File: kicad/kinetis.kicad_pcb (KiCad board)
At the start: 2 copper layers, 70 parts, among them J1 CONN_01X16, J2 CONN_01X16, J3 CONN_01X16, J4 CONN_01X16, J5 USB_Micro_B, J6 FTDI_Connector, J7 JLink_SWD_20pin, SW1 SPST, SW2 SPST, SW3 SPST, SW4 SPST, SW5 SPST, SW6 DPDT, U1 MKL16Z64VLH4, U2 LM1117-ADJ, Y1 12.000 MHz

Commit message: Lots of component placement. More to go.
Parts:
- moved C6 197.0 mm to (348.7, 85.3)
- moved R14 197.0 mm to (332.2, 112.0)
- moved R16 197.0 mm to (344.9, 96.8)
- moved R17 197.0 mm to (332.2, 122.2)
- moved R8 197.0 mm to (348.7, 117.1)
- moved C1 197.0 mm to (321.3, 132.3)
- moved C2 197.0 mm to (305.6, 86.6)
- moved C3 197.0 mm to (341.1, 86.6)
- moved R1 197.0 mm to (332.5, 106.9)
- moved R10 197.0 mm to (314.5, 134.9)
- moved R11 197.0 mm to (337.3, 98.0)
- moved R12 197.0 mm to (303.3, 106.9)
- moved R13 197.0 mm to (337.3, 91.7)
- moved R15 197.0 mm to (338.8, 123.4)
- moved R18 197.0 mm to (335.0, 117.1)
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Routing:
- added copper zone on F.Cu, net GND
- added copper zone on In1.Cu, net GND
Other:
- copper layers 2 -> 4

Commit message: Updated placement. More to go still.
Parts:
- moved R9 303.8 mm to (47.2, 128.3)
- moved R8 300.6 mm to (48.3, 123.7)
- moved C4 295.9 mm to (80.0, 75.4), turned to 90 degrees
- moved R7 293.4 mm to (48.3, 119.4)
- moved R16 273.0 mm to (73.9, 129.5)
- moved R22 269.8 mm to (61.7, 129.8)
- moved C6 269.1 mm to (80.0, 70.4), turned to 270 degrees
- moved R10 266.5 mm to (48.0, 132.1)
- moved R17 264.0 mm to (68.3, 129.5)
- moved R11 262.6 mm to (85.3, 24.1)
- moved C3 261.2 mm to (80.0, 78.2), turned to 270 degrees
- moved R6 258.8 mm to (93.5, 119.6)
- moved R21 256.8 mm to (55.9, 129.5)
- moved R13 245.7 mm to (94.0, 125.7)
- moved R14 239.0 mm to (94.0, 130.8)
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
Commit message: More placement and some preliminary routing
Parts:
- moved R10 84.7 mm to (110.7, 75.2)
- moved R14 77.6 mm to (83.2, 54.0)
- moved R8 77.0 mm to (110.7, 78.7)
- moved R9 76.6 mm to (110.7, 85.3)
- moved R13 75.3 mm to (75.6, 52.7)
- moved R7 72.7 mm to (110.7, 82.3)
- moved R6 51.9 mm to (110.1, 70.5)
- moved C12 38.7 mm to (64.8, 64.0), turned to 270 degrees
- moved C11 32.1 mm to (61.0, 63.8), turned to 270 degrees
- moved R5 29.8 mm to (110.5, 89.5)
- moved SW4 27.8 mm to (68.4, 128.4)
- moved R21 25.8 mm to (77.9, 116.0)
- moved R16 21.3 mm to (68.7, 108.8), turned to 180 degrees
- moved SW1 18.0 mm to (68.5, 114.0), turned to 180 degrees
- moved C10 17.5 mm to (47.0, 63.5), turned to 90 degrees
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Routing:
- net +3V3: track 0.00 -> 54.2 mm
- net GND: track 0.00 -> 13.3 mm, vias 0 -> 8
- net /SW[W]: track 0.00 -> 13.3 mm
- net /SW[E]: track 0.00 -> 11.6 mm
- net /SW[S]: track 0.00 -> 11.3 mm
- net /SW[N]: track 0.00 -> 10.8 mm
- net Net-(D4-PadK): track 0.00 -> 8.38 mm
- net Net-(D3-PadK): track 0.00 -> 8.38 mm
- net Net-(D2-PadK): track 0.00 -> 8.38 mm
- net Net-(D1-PadK): track 0.00 -> 8.38 mm
- added copper zone on B.Cu, net GND
- removed copper zone on F.Cu, net GND
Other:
- net class Default: clearance 0.2 -> 0.254; trace_width 0.25 -> 0.254; via_dia 0.6 -> 0.6096; via_drill 0.4 -> 0.3048
- rule trace_clearance: 0.2 -> 0.254
- rule trace_min: 0.2 -> 0.1524
- rule via_min_drill: 0.3 -> 0.3048
- rule via_min_size: 0.4 -> 0.6096
- board text added: "[0]"
- board text added: "[1]"
- board text added: "[2]"
- board text added: "[3]"

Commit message: Lots of layout and placement changes.
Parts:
- moved R11 90.4 mm to (170.2, 55.2)
- moved J6 87.9 mm to (96.5, 123.8)
- moved R1 87.9 mm to (106.7, 128.9)
- moved R2 87.9 mm to (102.9, 128.9)
- moved R3 87.9 mm to (99.1, 128.7)
- moved R4 87.9 mm to (110.5, 128.9)
- moved J7 84.9 mm to (174.6, 62.2)
- moved J5 83.1 mm to (123.8, 57.1)
- moved R12 82.9 mm to (164.5, 55.2)
- moved R6 79.6 mm to (176.5, 114.3), turned to 180 degrees
- moved R8 72.5 mm to (176.5, 109.2), turned to 180 degrees
- moved R7 72.1 mm to (176.5, 111.8), turned to 180 degrees
- moved R10 71.9 mm to (176.5, 104.1), turned to 180 degrees
- moved R5 71.5 mm to (176.5, 116.8), turned to 180 degrees
- moved R9 69.2 mm to (176.5, 106.7), turned to 180 degrees
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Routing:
- net /HEADER_C[3]: track 0.00 -> 33.8 mm
- net /HEADER_C[4]: track 0.00 -> 32.7 mm
- net /HEADER_C[5]: track 0.00 -> 30.9 mm
- net +3V3: track 54.2 -> 23.4 mm, vias 0 -> 3
- net /HEADER_C[6]: track 0.00 -> 29.3 mm
- net /HEADER_C[7]: track 0.00 -> 27.2 mm
- net /HEADER_C[8]: track 0.00 -> 26.2 mm
- net /HEADER_A[1]: track 0.00 -> 25.4 mm
- net /HEADER_D[16]: track 0.00 -> 25.2 mm
- net /HEADER_B[1]: track 0.00 -> 25.2 mm
- net /HEADER_D[1]: track 0.00 -> 24.8 mm
- net /HEADER_B[2]: track 0.00 -> 24.4 mm
- net /HEADER_D[15]: track 0.00 -> 24.0 mm
- net /HEADER_A[2]: track 0.00 -> 24.0 mm
- net /HEADER_D[2]: track 0.00 -> 24.0 mm
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
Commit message: Misc pin tweaks. Lots more routing.
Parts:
- removed R15, R18, R19, R20: 200, custom_footprints:SM_0805
- added C13: 0.1uF, custom_footprints:SM_0603, F.Cu at (132.1, 71.1)
- added C14: 0.1uF, custom_footprints:SM_0603, F.Cu at (124.5, 71.1)
- added C15: 0.1uF, custom_footprints:SM_0603, F.Cu at (177.3, 121.4)
- added C16: 0.1uF, custom_footprints:SM_0603, F.Cu at (174.8, 121.4)
- R13, R14, R5, R6: value 0.1 -> 200
- moved R11 32.1 mm to (142.2, 71.1), turned to 270 degrees
- moved R12 32.0 mm to (137.9, 73.2), turned to 270 degrees
- moved R27 27.9 mm to (140.0, 66.0), turned to 90 degrees
- moved R26 23.4 mm to (136.4, 65.5), turned to 90 degrees
- moved R16 21.3 mm to (101.5, 126.1)
- moved C9 20.2 mm to (112.0, 89.9), turned to 270 degrees
- moved C8 18.9 mm to (114.8, 90.7), turned to 270 degrees
- moved R2 18.3 mm to (109.2, 111.8)
- moved J6 17.9 mm to (101.6, 106.7)
- moved R1 17.9 mm to (111.8, 111.8)
- moved R3 17.6 mm to (104.1, 111.8)
- moved R4 17.6 mm to (114.3, 111.8)
- moved R22 13.9 mm to (104.0, 142.9)
- moved R23 13.6 mm to (102.1, 83.6), turned to 0 degrees
- moved D9 13.5 mm to (100.1, 100.6)
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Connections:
- D1 pad K: Net-(D1-PadK) -> GND
- D2 pad K: Net-(D2-PadK) -> GND
- D3 pad K: Net-(D3-PadK) -> GND
- D4 pad K: Net-(D4-PadK) -> GND
- R13 pad 1: /LED[2] -> /LED[3]
- R13 pad 2: /HEADER_D[15] -> /HEADER_D[16]
- R14 pad 1: /LED[3] -> /LED[2]
- R14 pad 2: /HEADER_D[16] -> /HEADER_D[15]
- R3 pad 2: /HEADER_B[12] -> /HEADER_B[13]
- R4 pad 2: /HEADER_B[13] -> /HEADER_B[12]
- R5 pad 1: /LED[0] -> /LED[1]
- R6 pad 1: /LED[1] -> /LED[0]
- R8 pad 1: /SW[S] -> /SW[E]
- R9 pad 1: /SW[E] -> /SW[S]
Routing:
- net JLink_nRST: track 0.00 -> 124.7 mm
- net /SW[W]: track 0.00 -> 122.1 mm
- net /LED[3]: track 0.00 -> 110.2 mm
- net /SW[E]: track 0.00 -> 96.4 mm
- net /LED[2]: track 0.00 -> 93.9 mm
- net /SW[S]: track 0.00 -> 86.7 mm
- net 5V_FTDI: track 0.00 -> 83.6 mm, vias 0 -> 1
- net /SW[N]: track 0.00 -> 81.2 mm
- net GND: track 26.1 -> 78.4 mm, vias 7 -> 29
- net /+4.6V: track 0.00 -> 44.9 mm
- net JLink_SWDIO: track 0.00 -> 44.0 mm
- net /HEADER_B[12]: track 22.1 -> 65.7 mm
- net JLink_SWCLK: track 0.00 -> 43.0 mm
- net /HEADER_B[13]: track 22.9 -> 64.9 mm
- net /LED[0]: track 3.33 -> 41.7 mm
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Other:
- net class Default: clearance 0.254 -> 0.2032
- rule trace_clearance: 0.254 -> 0.2032

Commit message: Routed some more stuff
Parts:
- moved J6 5.08 mm to (101.6, 111.8)
- moved R1 5.08 mm to (111.8, 116.8)
- moved R2 5.08 mm to (109.2, 116.8)
- moved R3 5.08 mm to (104.1, 116.8)
- moved R4 5.08 mm to (114.3, 116.8)
- moved J7 3.59 mm to (175.3, 66.0)
- moved R11 2.54 mm to (140.7, 73.2)
- moved R16 0.81 mm to (101.0, 126.7)
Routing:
- net /LED[2]: track 93.9 -> 154.2 mm
- net /LED[3]: track 110.2 -> 147.8 mm
- net /SW[N]: track 81.2 -> 110.3 mm
- net /SW[S]: track 86.7 -> 111.9 mm
- net /SW[W]: track 122.1 -> 146.2 mm
- net /HEADER_B[13]: track 64.9 -> 83.5 mm
- net /HEADER_A[9]: track 36.5 -> 52.1 mm
- net /HEADER_A[10]: track 30.8 -> 41.8 mm
- net JLink_SWCLK: track 43.0 -> 50.8 mm
- net /SW[E]: track 96.4 -> 103.6 mm
- net JLink_SWDIO: track 44.0 -> 50.6 mm
- net /HEADER_B[12]: track 65.7 -> 68.8 mm
- net 5V_FTDI: track 83.6 -> 80.7 mm
- net +3V3: track 27.1 -> 29.6 mm, vias 3 -> 5
- net /HEADER_D[13]: track 33.1 -> 32.4 mm

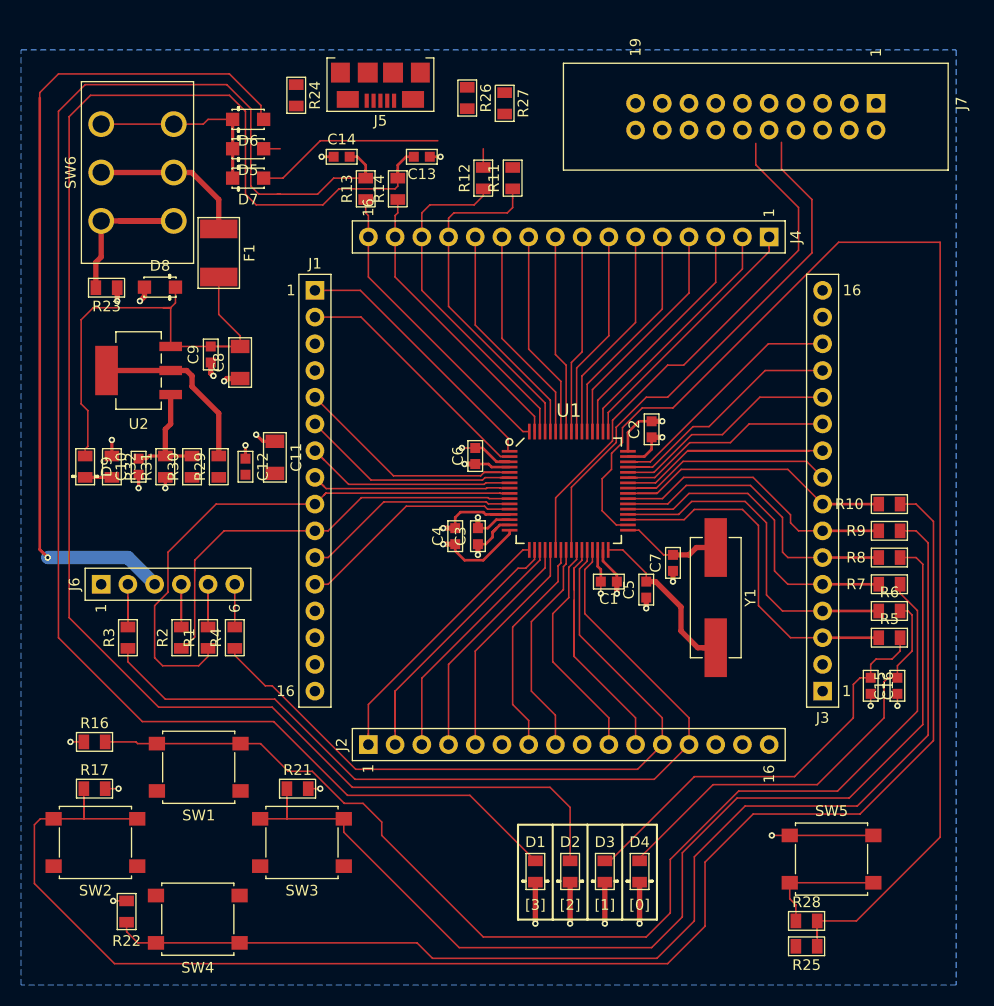
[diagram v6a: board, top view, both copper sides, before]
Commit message: Added mounting holes. Moved stuff. More routing.
This commit adds 4-40 mounting holes to the design, and shoves
a bunch of stuff around to make room for them. It also moves
the DPDT switch to ignore the secondary switch pole, in order to make
some routing space.
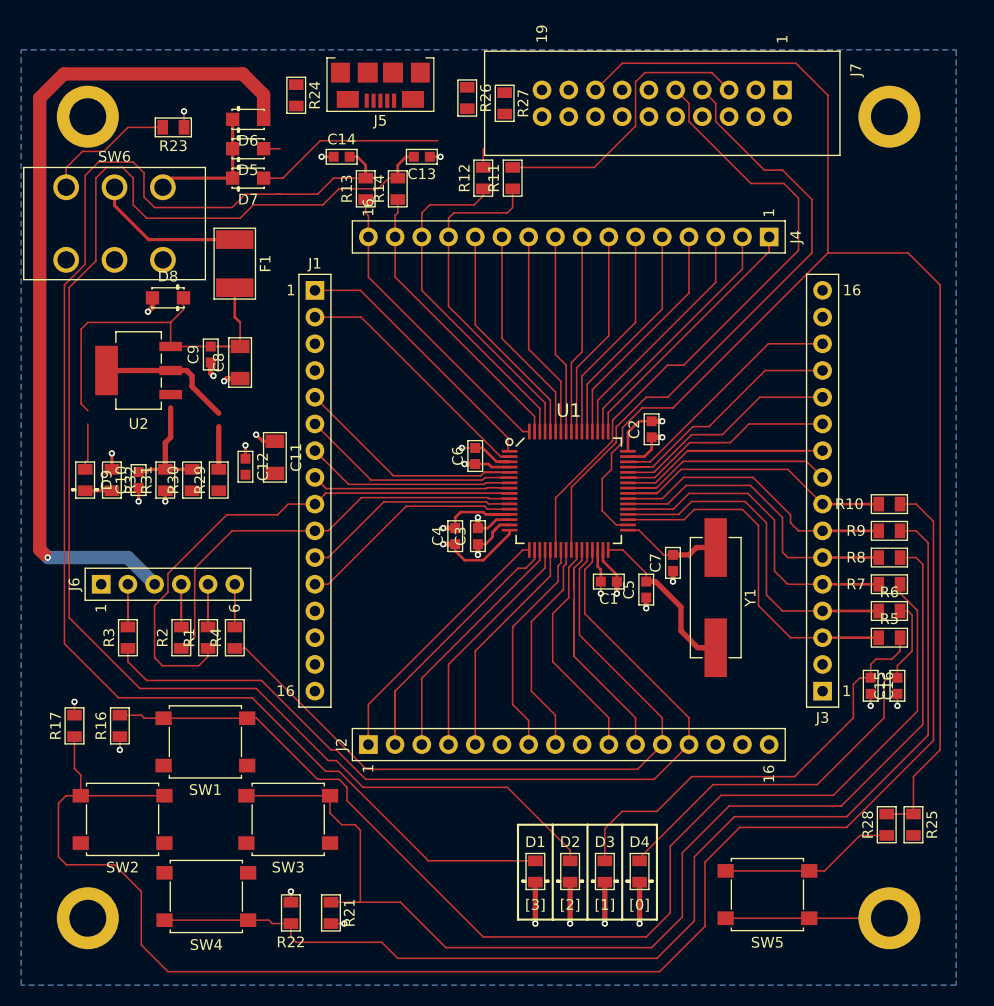
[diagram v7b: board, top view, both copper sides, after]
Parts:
- added M1: #4-40 Mounting Hole, custom_footprints:4_40_Hole, F.Cu at (176.5, 143.5)
- added M2: #4-40 Mounting Hole, custom_footprints:4_40_Hole, F.Cu at (100.3, 143.5)
- added M3: #4-40 Mounting Hole, custom_footprints:4_40_Hole, F.Cu at (100.3, 67.3)
- added M4: #4-40 Mounting Hole, custom_footprints:4_40_Hole, F.Cu at (176.5, 67.3)
- moved R23 16.5 mm to (108.5, 68.3)
- moved R22 15.6 mm to (119.6, 143.0)
- moved R25 15.4 mm to (178.8, 134.6), turned to 90 degrees
- moved R21 12.2 mm to (123.4, 143.0), turned to 270 degrees
- moved R28 11.9 mm to (176.3, 134.6), turned to 270 degrees
- moved J7 8.98 mm to (166.4, 64.8)
- moved SW5 6.97 mm to (164.9, 141.3), turned to 180 degrees
- moved R17 6.27 mm to (99.1, 125.2), turned to 90 degrees
- moved SW6 5.32 mm to (102.9, 77.5), turned to 0 degrees
- moved SW2 3.39 mm to (103.6, 134.1)
- moved R16 2.85 mm to (103.4, 125.2), turned to 270 degrees
- moved SW3 2.56 mm to (119.4, 134.1)
- moved SW1 2.50 mm to (111.5, 126.7)
- moved SW4 2.31 mm to (111.6, 141.4)
- moved F1 1.83 mm to (114.3, 81.3)
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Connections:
- SW6 pad A2: Net-(R23-Pad1) -> Net-(SW6-PadA2)
- SW6 pad B2: Net-(F1-Pad2) -> Net-(SW6-PadB2)
- SW6 pad C2: Net-(D5-PadK) -> Net-(SW6-PadC2)
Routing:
- net JLink_Tx: track 0.00 -> 27.4 mm
- net JLink_nRST: track 124.7 -> 143.3 mm
- net /LED[2]: track 154.2 -> 138.7 mm
- net /LED[3]: track 147.8 -> 134.2 mm
- net JLink_SWCLK: track 50.8 -> 60.9 mm
- net JLink_SWDIO: track 50.6 -> 59.7 mm
- net GND: track 78.2 -> 87.1 mm, vias 29 -> 28
- net Net-(R23-Pad1): track 18.6 -> 12.6 mm
- net Net-(D5-PadK): track 18.0 -> 12.6 mm
- net Net-(R28-Pad2): track 11.8 -> 16.7 mm
- net /SW[E]: track 103.6 -> 108.1 mm
- net /+4.6V: track 44.9 -> 40.5 mm
- net /SW[S]: track 111.9 -> 108.6 mm
- net /SW[W]: track 146.2 -> 149.4 mm
- net /LED[1]: track 40.2 -> 42.0 mm
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
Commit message: More routing fun!
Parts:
- moved R12 6.88 mm to (144.8, 72.6), turned to 180 degrees
- moved R27 5.57 mm to (134.9, 68.3), turned to 0 degrees
- moved R11 4.73 mm to (144.8, 75.6), turned to 180 degrees
- moved C13 2.90 mm to (132.8, 73.9), turned to 270 degrees
- moved C14 2.90 mm to (123.7, 73.9), turned to 270 degrees
- moved J5 1.94 mm to (126.2, 62.7)
- moved R26 1.55 mm to (134.9, 65.3), turned to 0 degrees
- moved R24 1.27 mm to (119.4, 64.3)
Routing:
- net 5V_USB: track 1.52 -> 41.8 mm
- net GND: track 87.1 -> 108.9 mm, vias 28 -> 31
- net 5V_JLink: track 18.0 -> 32.3 mm
- net Net-(J5-Pad2): track 0.00 -> 12.7 mm
- net Net-(J5-Pad3): track 0.00 -> 9.94 mm
- net Net-(J5-Pad4): track 0.00 -> 9.54 mm
- net JLink_Rx: track 1.78 -> 9.02 mm
- net /HEADER_D[14]: track 32.6 -> 38.5 mm
- net /LED[3]: track 134.2 -> 130.8 mm
- net JLink_Tx: track 27.4 -> 24.9 mm
- net /HEADER_D[13]: track 32.4 -> 34.1 mm
